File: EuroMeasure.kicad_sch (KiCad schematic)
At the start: 66 parts, among them SW1 SW_DIP_x04, SW2 RST, U3 AZ1117-3V3, U4 STM32G030CxT, Y1 16MHz

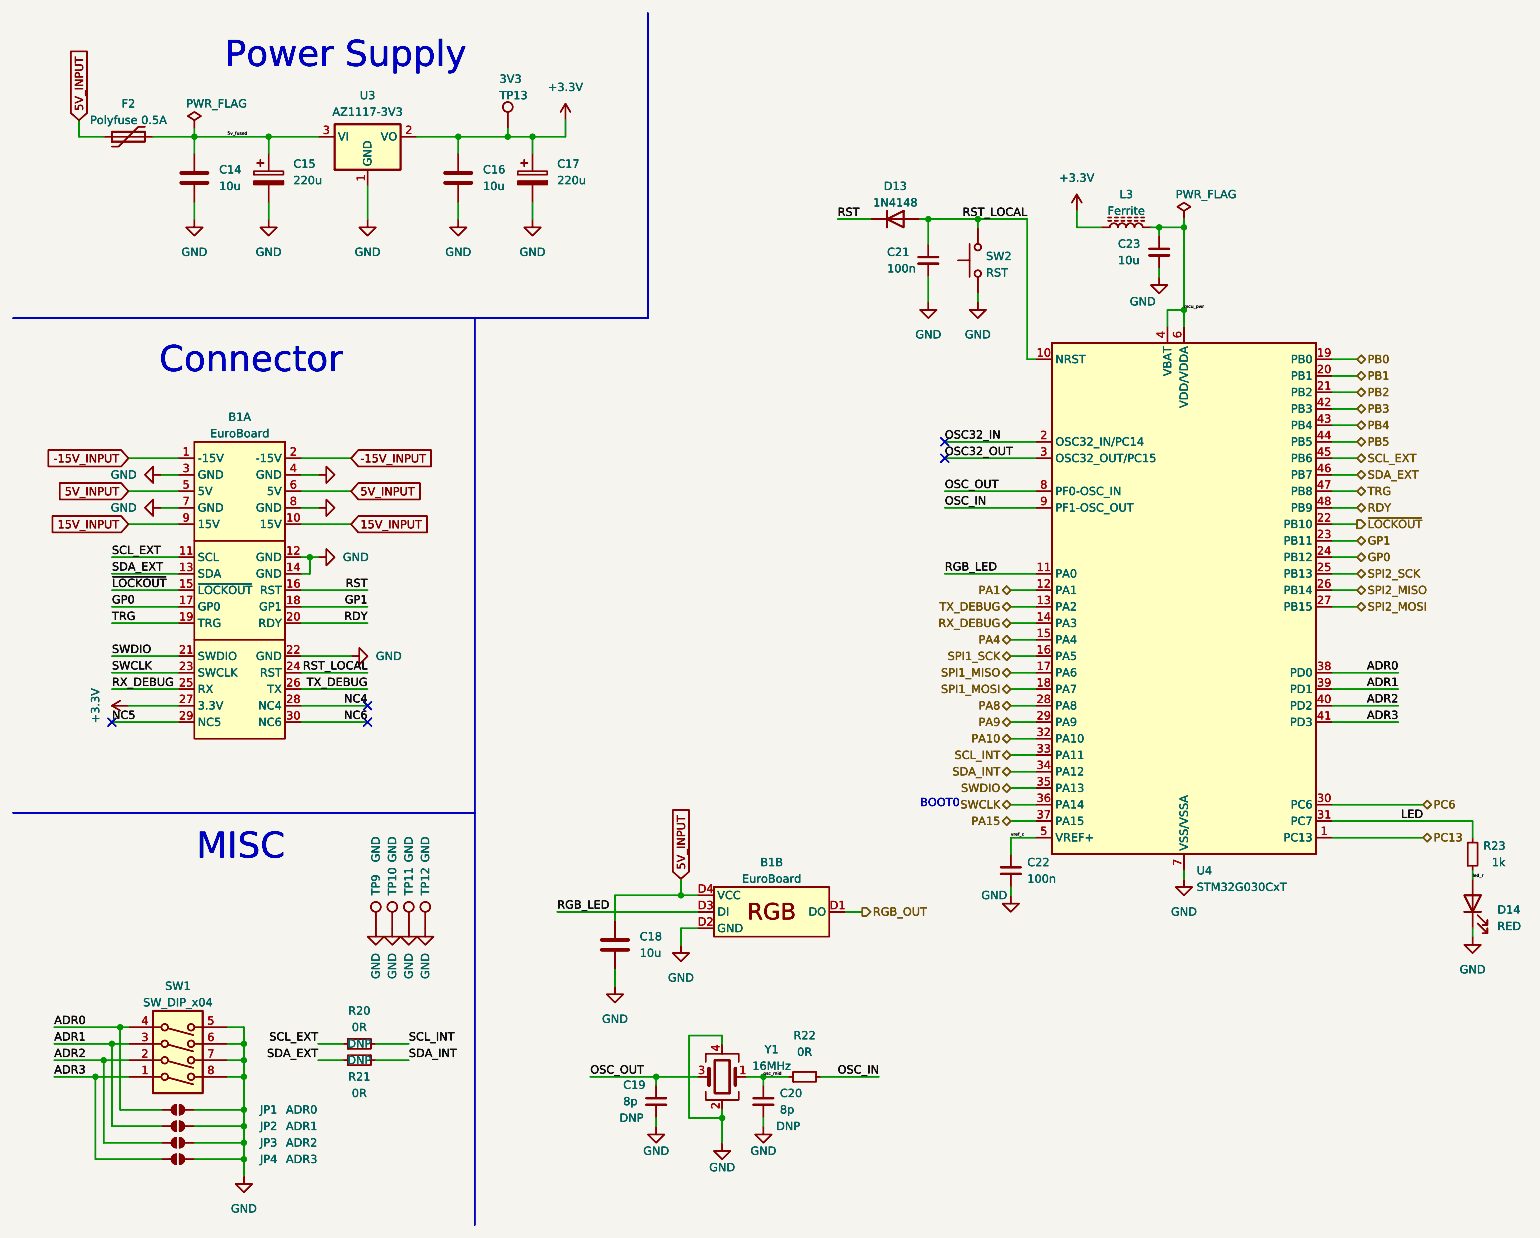
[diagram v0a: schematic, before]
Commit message: Reverted duplicated components
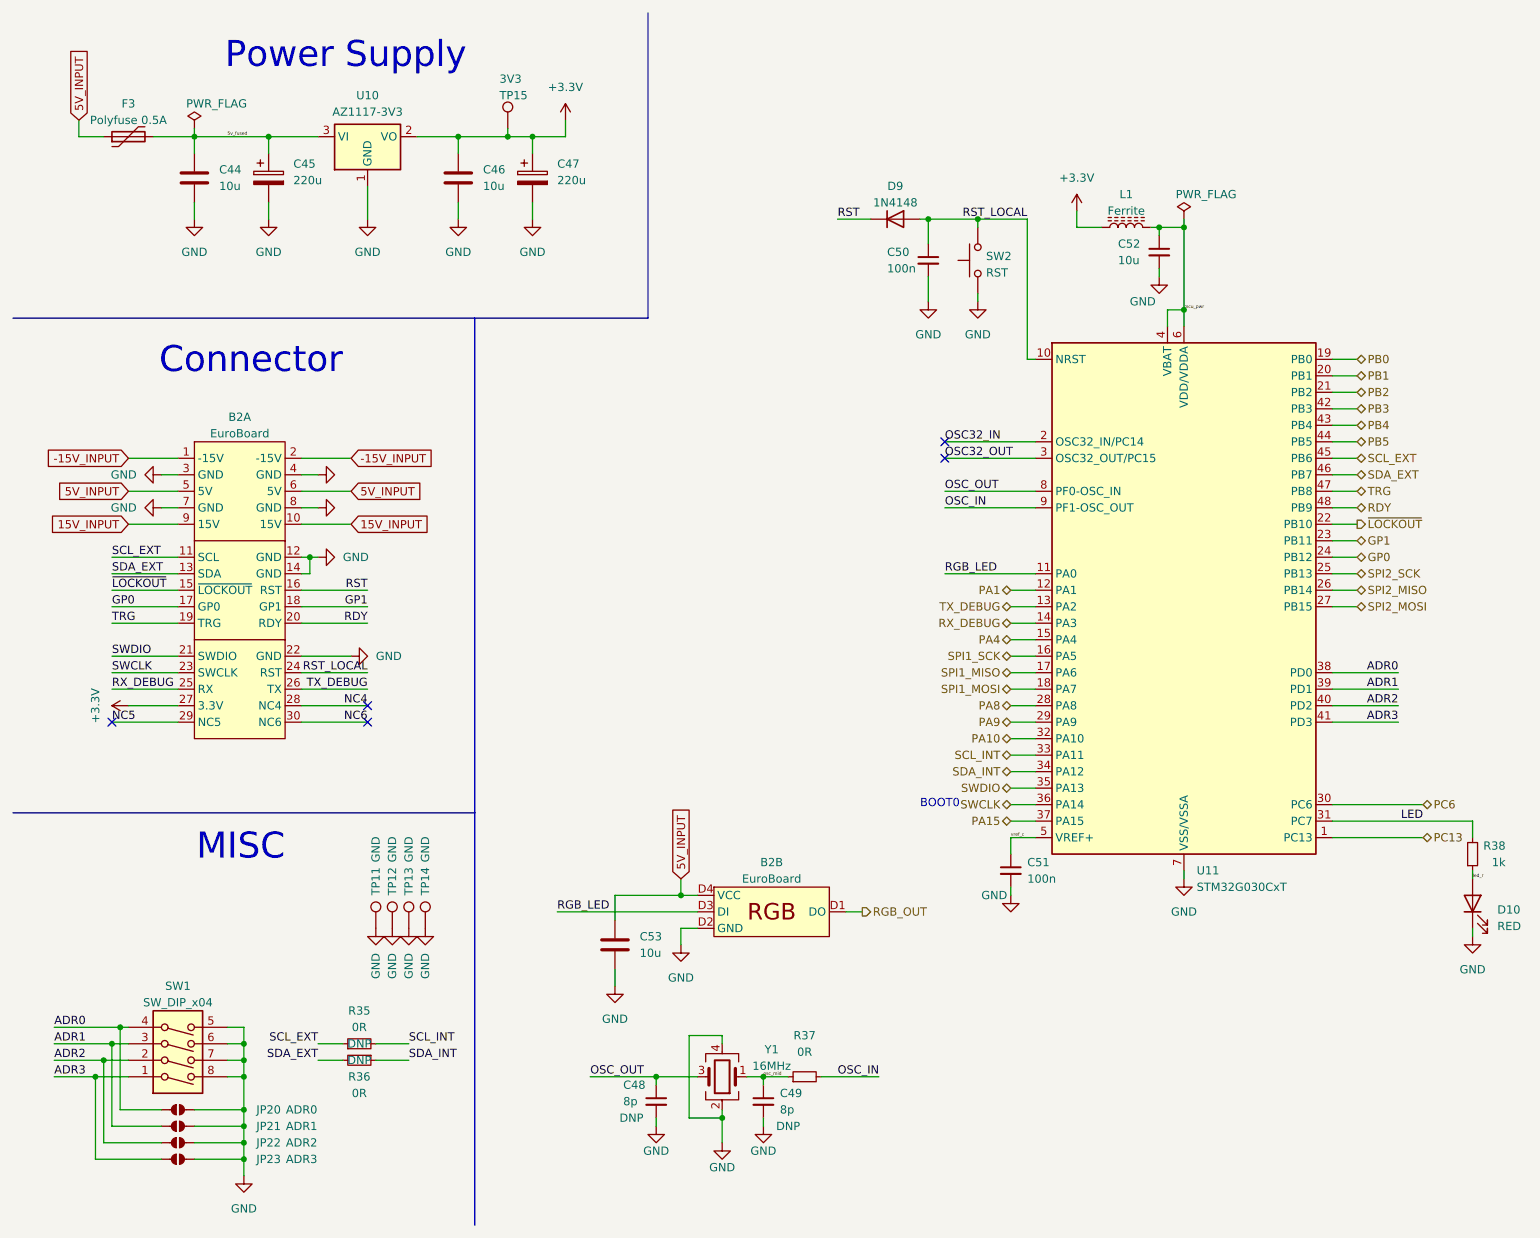
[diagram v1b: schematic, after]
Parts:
- removed B1: EuroBoard, MEMS_Custom:EuroMeasureLED, symbol MEMS_Custom:EuroBoardLED
- removed C14, C16, C18: 10u, Capacitor_SMD:C_0805_2012Metric_Pad1.18x1.45mm_HandSolder, symbol Device:C
- removed C15, C17: 220u, Capacitor_SMD:CP_Elec_6.3x7.7, symbol Device:C_Polarized
- removed C19, C20: 8p, Capacitor_SMD:C_0805_2012Metric_Pad1.18x1.45mm_HandSolder, symbol Device:C_Small
- removed C21, C22: 100n, Capacitor_SMD:C_0805_2012Metric_Pad1.18x1.45mm_HandSolder, symbol Device:C_Small
- removed C23: 10u, Capacitor_SMD:C_0805_2012Metric_Pad1.18x1.45mm_HandSolder, symbol Device:C_Small
- removed D13: 1N4148, Diode_SMD:D_SOD-323F, symbol MEMS_Discrete-semiconductor:D_1N4148WS-SOD323
- removed D14: RED, LED_SMD:LED_0805_2012Metric_Pad1.15x1.40mm_HandSolder, symbol MEMS_Discrete-semiconductor:LED_0805_Red
- removed F2: Polyfuse 0.5A, Fuse:Fuse_1210_3225Metric, symbol MEMS_Protection:Polyfuse-500mA-1206L050/15YR
- removed JP1: ADR0, MEMS_Passive:R_0805_2012Metric_Jumper, symbol MEMS_Passive:SolderableJumper
- removed JP2: ADR1, MEMS_Passive:R_0805_2012Metric_Jumper, symbol MEMS_Passive:SolderableJumper
- removed JP3: ADR2, MEMS_Passive:R_0805_2012Metric_Jumper, symbol MEMS_Passive:SolderableJumper
- removed JP4: ADR3, MEMS_Passive:R_0805_2012Metric_Jumper, symbol MEMS_Passive:SolderableJumper
- removed L3: Ferrite, Inductor_SMD:L_0805_2012Metric_Pad1.15x1.40mm_HandSolder, symbol MEMS_Passive:L_Ferrite_742792040
- removed R20, R21, R22: 0R, Capacitor_SMD:C_0805_2012Metric_Pad1.18x1.45mm_HandSolder, symbol Device:R_Small
- removed R23: 1k, Resistor_SMD:R_0805_2012Metric_Pad1.20x1.40mm_HandSolder, symbol Device:R_Small
- removed SW1: SW_DIP_x04, Button_Switch_SMD:SW_DIP_SPSTx04_Slide_Omron_A6H-4101_W6.15mm_P1.27mm, symbol MEMS_Electromechanical:SW_DIP_A6H-4101
- removed SW2: RST, Button_Switch_SMD:SW_SPST_B3S-1000, symbol MEMS_Electromechanical:SW_Push_Tact_B3S-1000
- removed TP10, TP11, TP12, TP9: GND, MEMS_Custom:TestPoint_Pad_D1.0mm, symbol Connector:TestPoint
- removed TP13: 3V3, MEMS_Custom:TestPoint_Pad_D1.0mm, symbol Connector:TestPoint
- removed U3: AZ1117-3V3, Package_TO_SOT_SMD:SOT-223-3_TabPin2, symbol MEMS_IC:AZ1117IH-3.3TRG1-SOT223
- removed U4: STM32G030CxT, Package_QFP:LQFP-48_7x7mm_P0.5mm, symbol MEMS_IC:STM32G030CxT
- removed Y1: 16MHz, Oscillator:Oscillator_SMD_Abracon_ASDMB-4Pin_2.5x2.0mm, symbol MEMS_Passive:Crystal_16MHz_ECS-160-8-36CKM-TR3
- renumbered B1 to B2, C14 to C44, C15 to C45, C16 to C46, C17 to C47, C19 to C48, C20 to C49, C21 to C50, C22 to C51, C23 to C52, C18 to C53, D14 to D10, D13 to D9, F2 to F3, JP1 to JP20, JP2 to JP21, JP3 to JP22, JP4 to JP23, L3 to L1, R20 to R35, R21 to R36, R22 to R37, R23 to R38, TP9 to TP11, TP10 to TP12, TP11 to TP13, TP12 to TP14, TP13 to TP15, U3 to U10, U4 to U11
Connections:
- no-connect marks 10 -> 5

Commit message: Reverted duplicated components
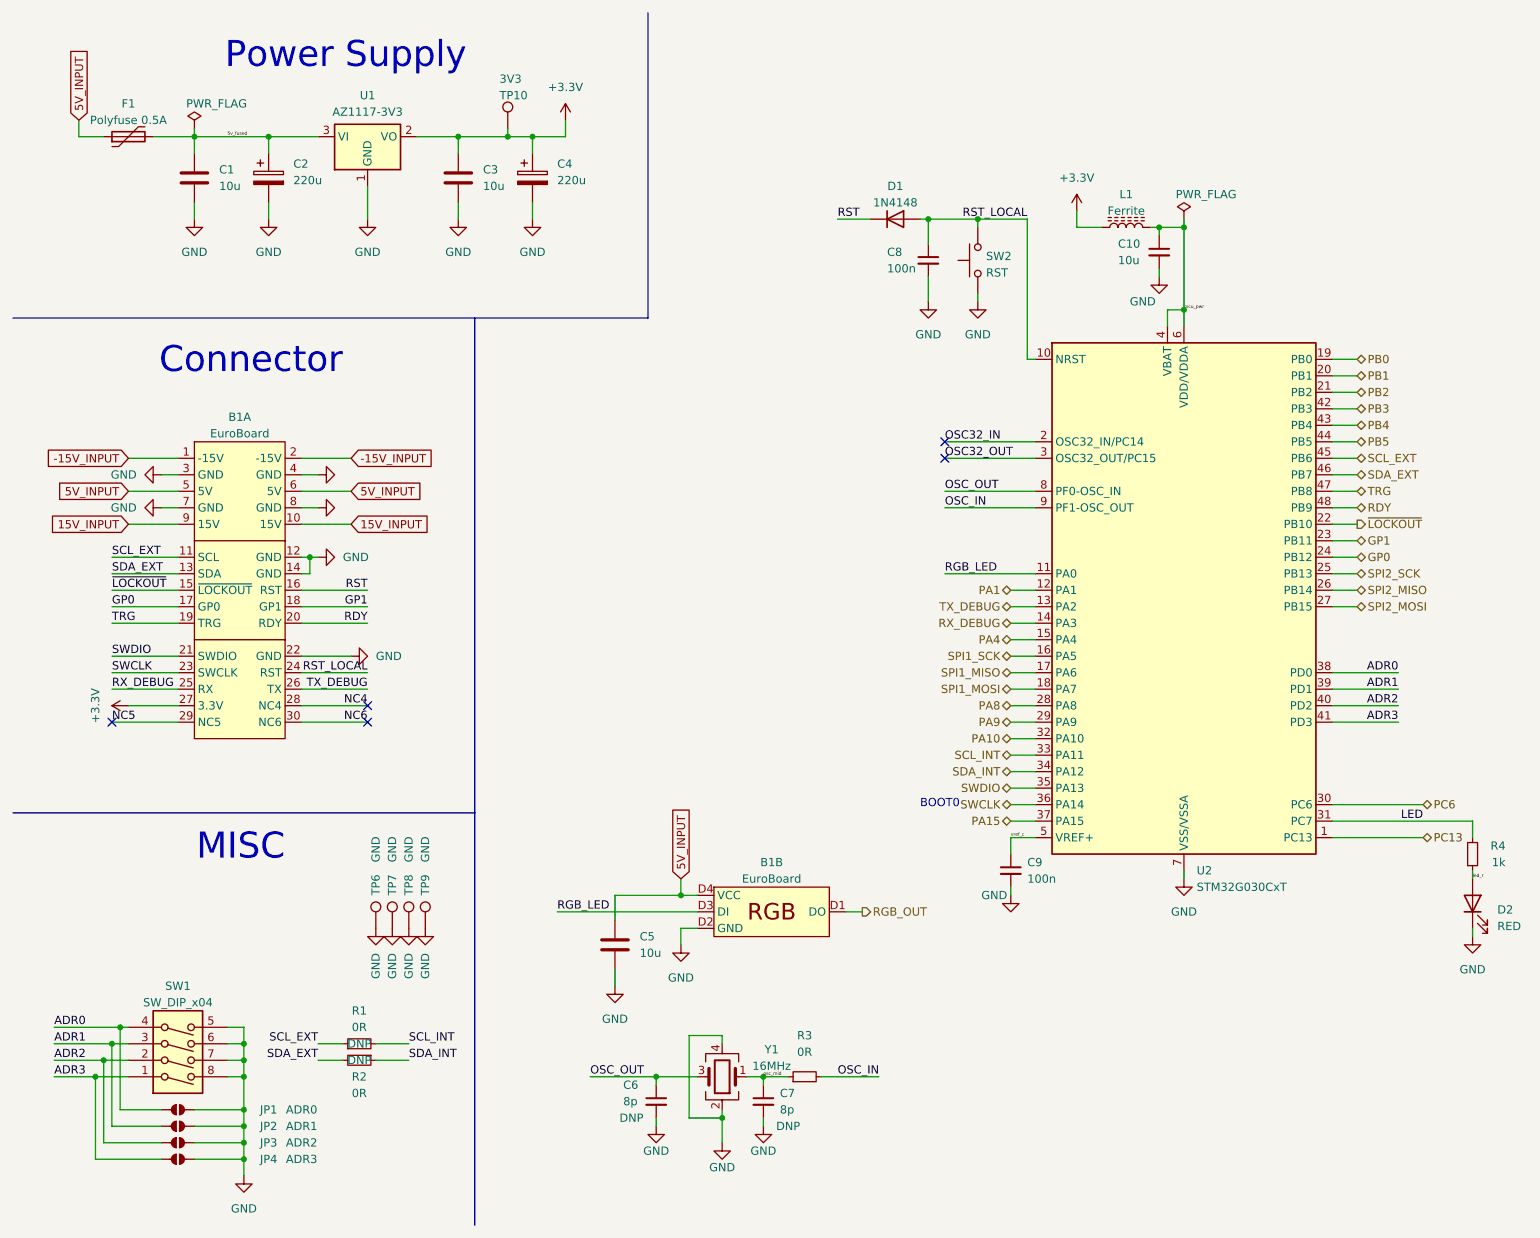
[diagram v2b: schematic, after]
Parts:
- renumbered B2 to B1, C44 to C1, C52 to C10, C45 to C2, C46 to C3, C47 to C4, C53 to C5, C48 to C6, C49 to C7, C50 to C8, C51 to C9, D9 to D1, D10 to D2, F3 to F1, JP20 to JP1, JP21 to JP2, JP22 to JP3, JP23 to JP4, R35 to R1, R36 to R2, R37 to R3, R38 to R4, TP15 to TP10, TP11 to TP6, TP12 to TP7, TP13 to TP8, TP14 to TP9, U10 to U1, U11 to U2

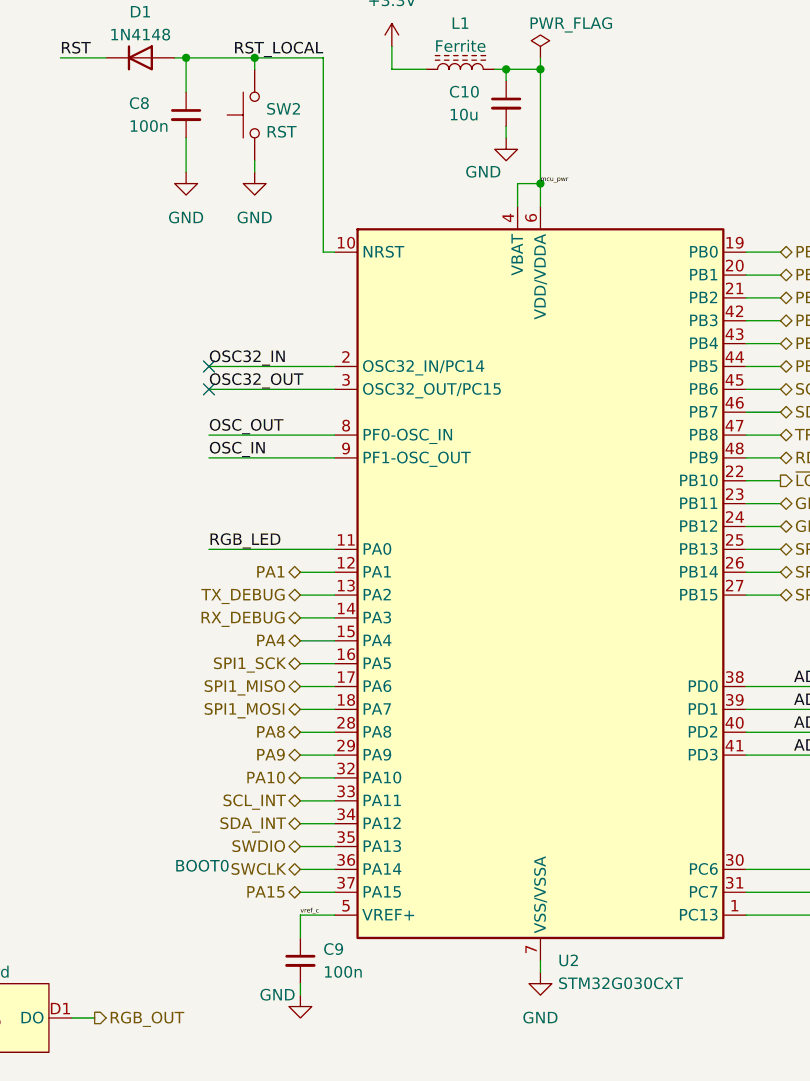
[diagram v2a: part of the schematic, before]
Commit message: Fixed VREF
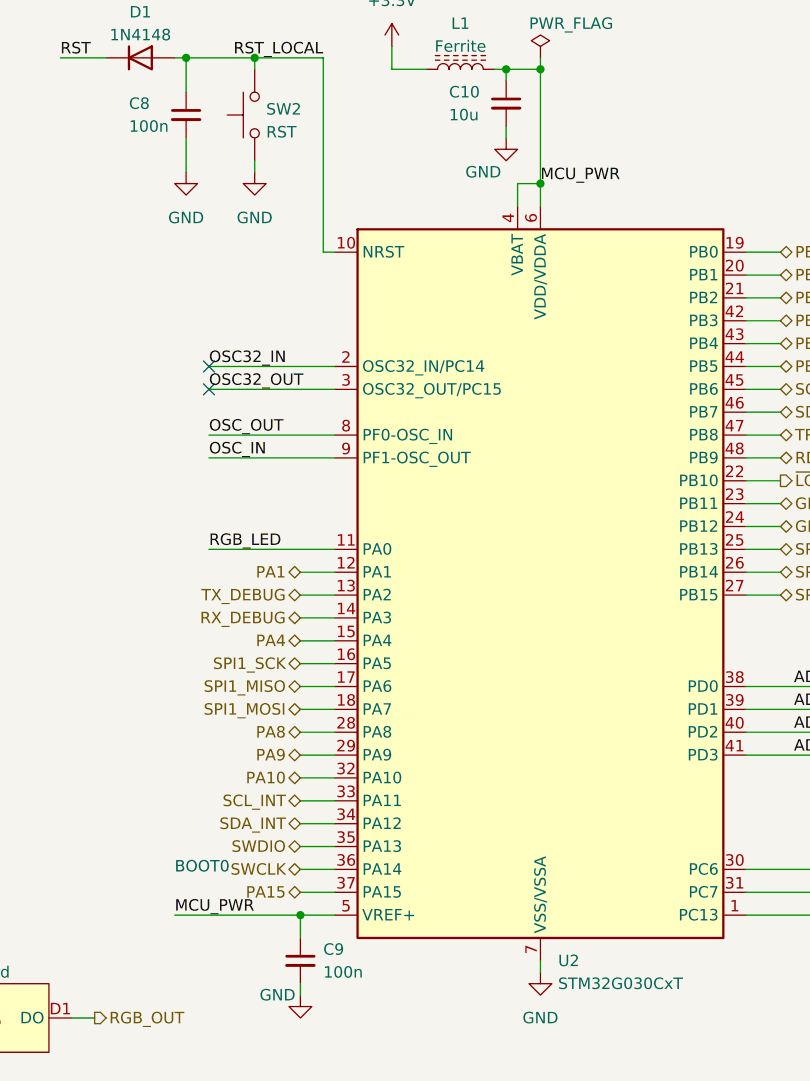
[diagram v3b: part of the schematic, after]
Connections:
- net vref_c is gone; now on net MCU_PWR: C9.1, U2.5 (VREF+)
- net mcu_pwr renamed MCU_PWR
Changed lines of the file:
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@@
   (junction (at 39.37 30.48) (diameter 0) (color 0 0 0 0)
+  )
+  (junction (at 165.1 138.43) (diameter 0) (color 0 0 0 0)
   )
   (junction (at 24.13 175.26) (diameter 0) (color 0 0 0 0)
@@
     (stroke (width 0) (type default))
   )
+  (wire (pts (xy 151.13 138.43) (xy 165.1 138.43))
+    (stroke (width 0) (type default))
+  )
   (wire (pts (xy 55.88 85.09) (xy 63.5 85.09))
     (stroke (width 0) (type default))
@@
     (effects (font (size 1.27 1.27)) (justify left bottom))
   )
-  (label "mcu_pwr" (at 191.77 57.15 0) (fields_autoplaced)
-    (effects (font (size 0.5 0.5)) (justify left bottom))
+  (label "MCU_PWR" (at 191.77 57.15 0) (fields_autoplaced)
+    (effects (font (size 1.27 1.27)) (justify left bottom))
   )
   (label "RST_LOCAL" (at 167.64 43.18 180) (fields_autoplaced)
@@
     (effects (font (size 1.27 1.27)) (justify right bottom))
   )
+  (label "MCU_PWR" (at 151.13 138.43 0) (fields_autoplaced)
+    (effects (font (size 1.27 1.27)) (justify left bottom))
+  )
   (label "SDA_INT" (at 72.39 172.72 0) (fields_autoplaced)
     (effects (font (size 1.27 1.27)) (justify left bottom))
@@
     (effects (font (size 1.27 1.27)) (justify left bottom))
   )
-  (label "vref_c" (at 165.1 138.43 0) (fields_autoplaced)
-    (effects (font (size 0.5 0.5)) (justify left bottom))
-  )
   (label "ADR2" (at 17.78 172.72 0) (fields_autoplaced)
